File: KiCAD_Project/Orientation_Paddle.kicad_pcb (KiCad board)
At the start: 2 copper layers, 110.5 x 47 mm, 67 parts, among them J1 1-0001205, J2 1-0001156, J3 1-0001156, J4 NP_Conn_01x02_Relief, J5 NP_Conn_01x02_Relief, J6 NP_Conn_01x04, J7 NP_Conn_01x02, J8 1-0000050, J9 1-0000190, Q1 1-0001670, U1 1-0001471, U2 1-0000207, U3 1-0000785, U4 1-0000446, Y1 1-0000721

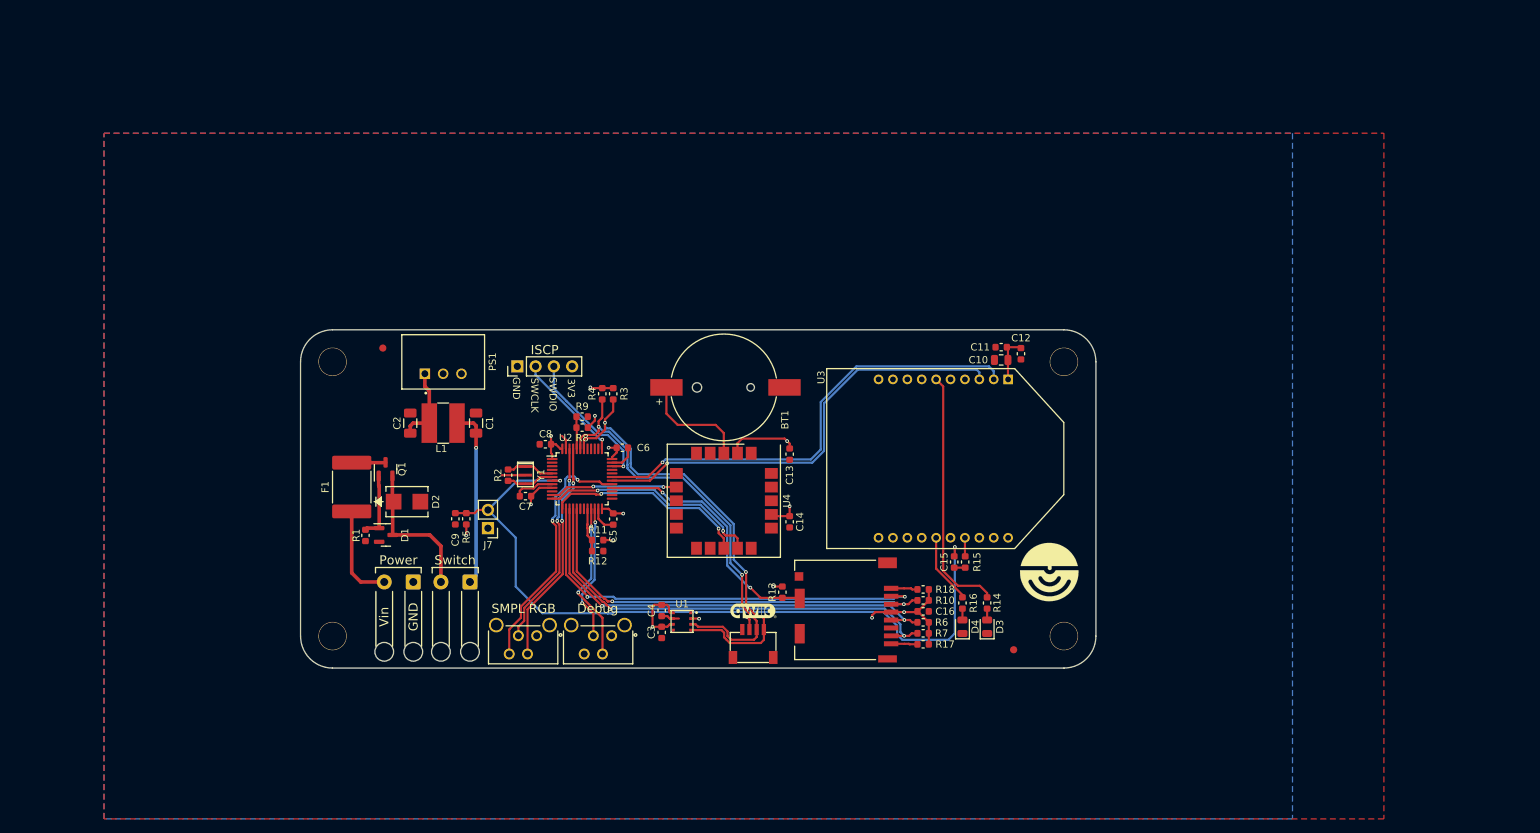
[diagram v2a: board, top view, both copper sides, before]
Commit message: Fixed Issues #9, Issue #10 (Rev2.1)
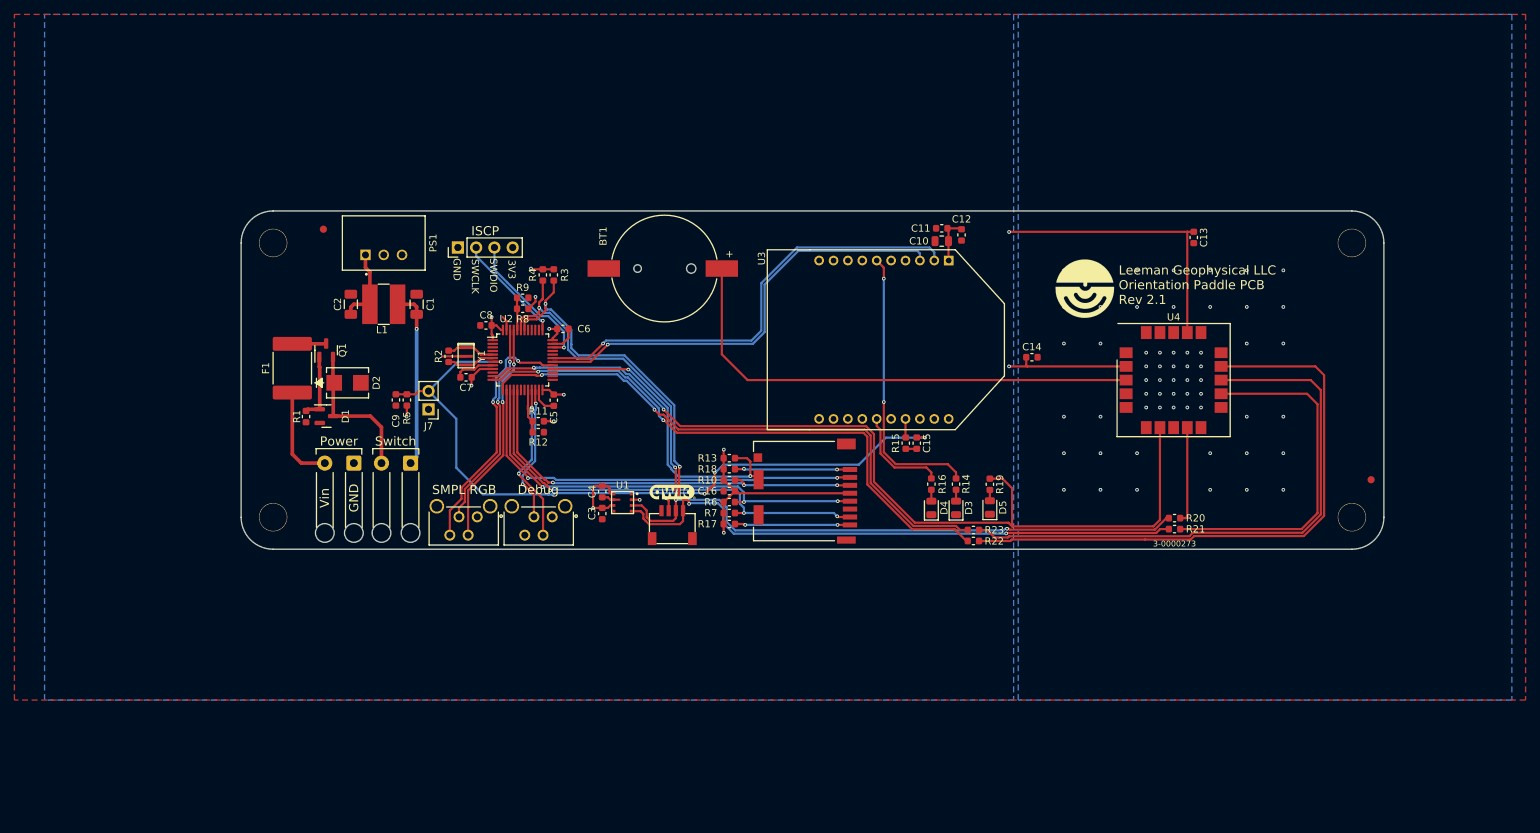
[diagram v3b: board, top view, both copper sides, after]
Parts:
- removed the G*** at (175.8, 130.8)
- added D5: 1-0000601, leds_0805:1-0000601, F.Cu at (167.5, 121.8)
- added R19: 1-0000008, resistors_0603:1-0000008, F.Cu at (167.5, 118.6)
- added R20: 1-0000006, resistors_0603:1-0000006, F.Cu at (193.2, 123.3)
- added R21: 1-0000006, resistors_0603:1-0000006, F.Cu at (193.2, 124.8)
- added R22: 1-0000006, resistors_0603:1-0000006, F.Cu at (165.2, 126.5)
- added R23: 1-0000006, resistors_0603:1-0000006, F.Cu at (165.2, 125.0)
- G***: moved to F.Cu
- moved U4 64.7 mm to (193.0, 104.1), turned to 0 degrees
- moved C13 63.7 mm to (195.8, 84.3)
- moved FID1 55.0 mm to (220.5, 118.0)
- moved G*** 48.8 mm to (180.7, 91.4), turned to 0 degrees
- moved H2 43.3 mm to (217.8, 123.2)
- moved H4 43.3 mm to (217.8, 85.1)
- moved C14 40.7 mm to (173.4, 101.0), turned to 0 degrees
- moved R10 31.7 mm to (131.3, 118.0), turned to 0 degrees
- moved R18 31.7 mm to (131.3, 116.5), turned to 0 degrees
- moved R17 31.7 mm to (131.3, 124.1), turned to 0 degrees
- moved R6 31.7 mm to (131.3, 121.1), turned to 0 degrees
- moved R7 31.7 mm to (131.3, 122.6), turned to 0 degrees
- moved C16 31.7 mm to (131.3, 119.6), turned to 0 degrees
- moved R13 20.0 mm to (131.3, 115.0), turned to 0 degrees
- moved G*** 20.0 mm to (123.4, 119.6)
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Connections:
- U4 pad 12: unconnected-(U4-SCL-Pad12) -> Net-(U4-SCL)
- U4 pad 13: GPS_TX -> Net-(U4-TXD)
- U4 pad 14: GPS_RX -> Net-(U4-RXD)
- U4 pad 9: unconnected-(U4-SDA-Pad9) -> Net-(U4-SDA)
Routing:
- net GPS_PPS: track 17.8 -> 128.6 mm
- net Net-(U4-RXD): track 0.00 -> 83.7 mm
- net Net-(U4-TXD): track 0.00 -> 80.9 mm
- net SDA: track 62.1 -> 130.3 mm, vias 2 -> 4
- net SCL: track 64.7 -> 131.3 mm, vias 2 -> 4
- net +3V3: track 74.4 -> 129.7 mm, vias 16 -> 15
- net Net-(BT1-+): track 15.5 -> 69.6 mm
- net GPS_TX: track 28.4 -> 79.0 mm
- net GPS_RX: track 30.9 -> 80.8 mm
- net Net-(U4-SCL): track 0.00 -> 49.1 mm
- net Net-(U4-SDA): track 0.00 -> 13.4 mm
- net Net-(J9-DAT1): track 3.69 -> 16.0 mm, vias 0 -> 2
- net Net-(J9-DAT2): track 3.72 -> 16.0 mm, vias 0 -> 2
- net SD_CD: track 35.5 -> 44.0 mm
- net Reset: track 108.5 -> 102.0 mm, vias 2 -> 4
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- added copper zone on B.Cu, net GND
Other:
- board size 110.5 x 47 mm -> 158.7 x 47 mm
- board text added: "3-0000273"
- board text added: "Leeman Geophysical LLC Orientation Paddle PCB Rev 2.1"
- board text removed: "3-0000267"
- board text removed: "Leeman Geophysical LLC Orientation Paddle PCB Rev 2.0"

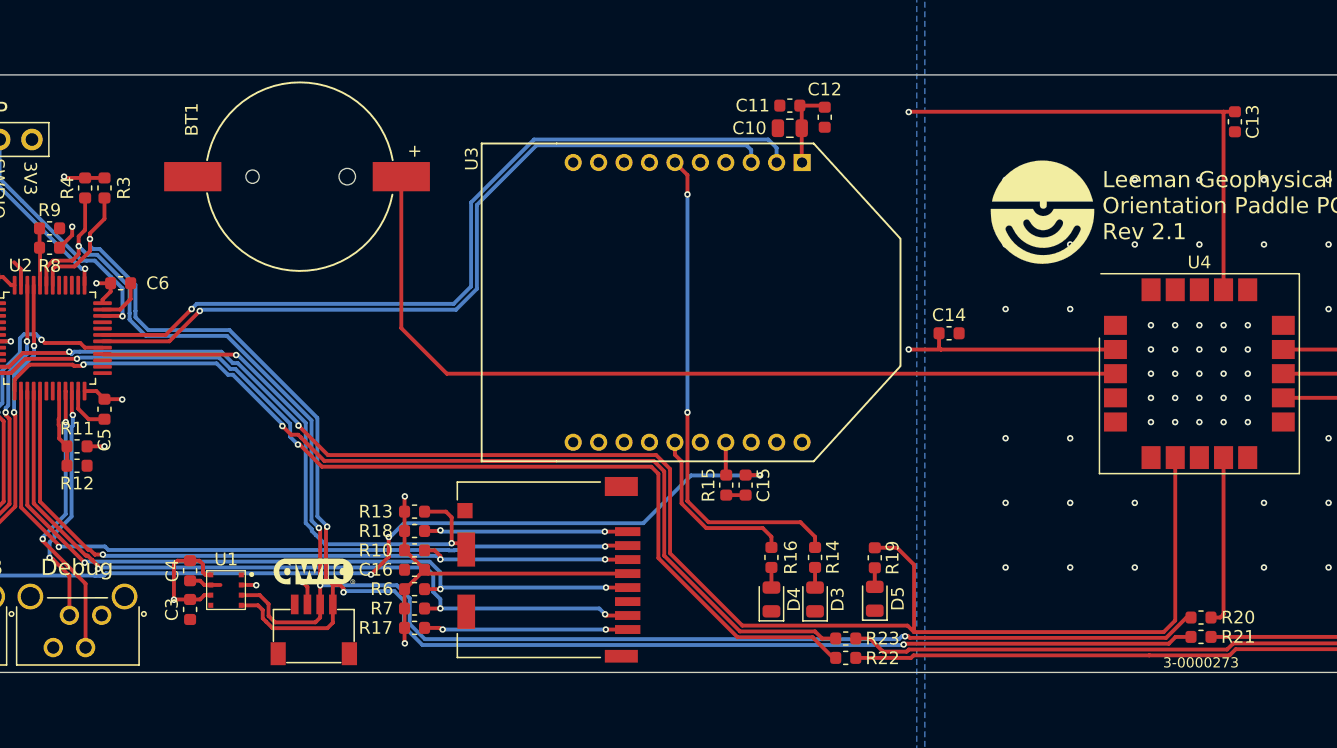
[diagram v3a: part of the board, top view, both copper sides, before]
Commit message: Add serial jumpers for GPS and make production files for Rev 2.1
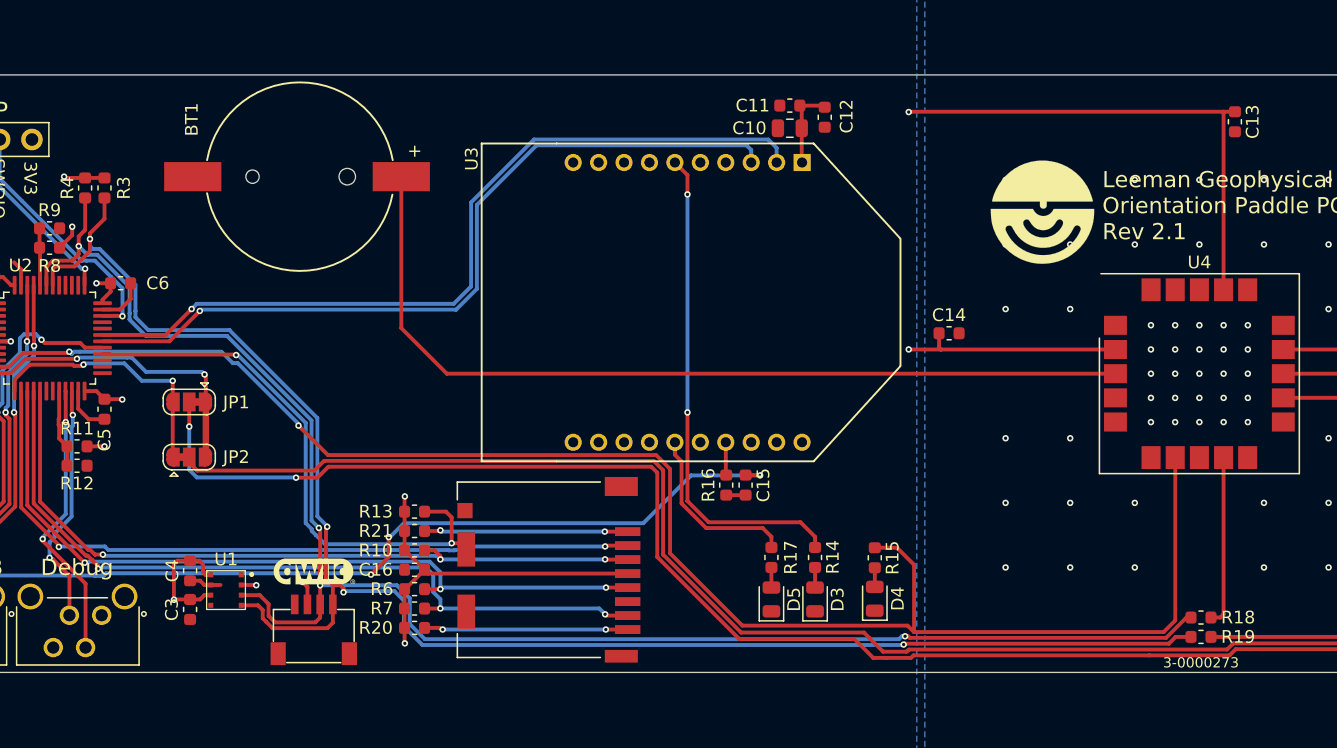
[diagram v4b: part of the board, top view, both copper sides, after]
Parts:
- removed R22, R23: 1-0000006, resistors_0603:1-0000006
- added JP1: SolderJumper_3_Bridged12, np_connectors:SolderJumper-3_P1.3mm_Bridged12_RoundedPad1.0x1.5mm, F.Cu at (113.6, 106.4)
- added JP2: SolderJumper_3_Bridged12, np_connectors:SolderJumper-3_P1.3mm_Bridged12_RoundedPad1.0x1.5mm, F.Cu at (113.6, 110.7)
- renumbered D5 to D4, D4 to D5, R19 to R15, R15 to R16, R16 to R17, R20 to R18, R21 to R19, R17 to R20, R18 to R21
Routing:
- net Net-(JP1-C): track 83.7 -> 152.2 mm, vias 0 -> 2
- net Net-(JP2-C): track 80.9 -> 144.0 mm
- net GPS_TX: track 79.0 -> 20.5 mm
- net GPS_RX: track 80.8 -> 23.9 mm
